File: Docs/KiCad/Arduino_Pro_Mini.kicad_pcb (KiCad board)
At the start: 2 copper layers, 47 x 95.2 mm, 19 parts, among them P1 Digital, P2 COM, P3 ADC, P4 Analog, P5 ADC, P6 COM, P7 CONN_01X04, P8 CONN_01X03, P9 CONN_01X04, SW1 SW_PUSH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

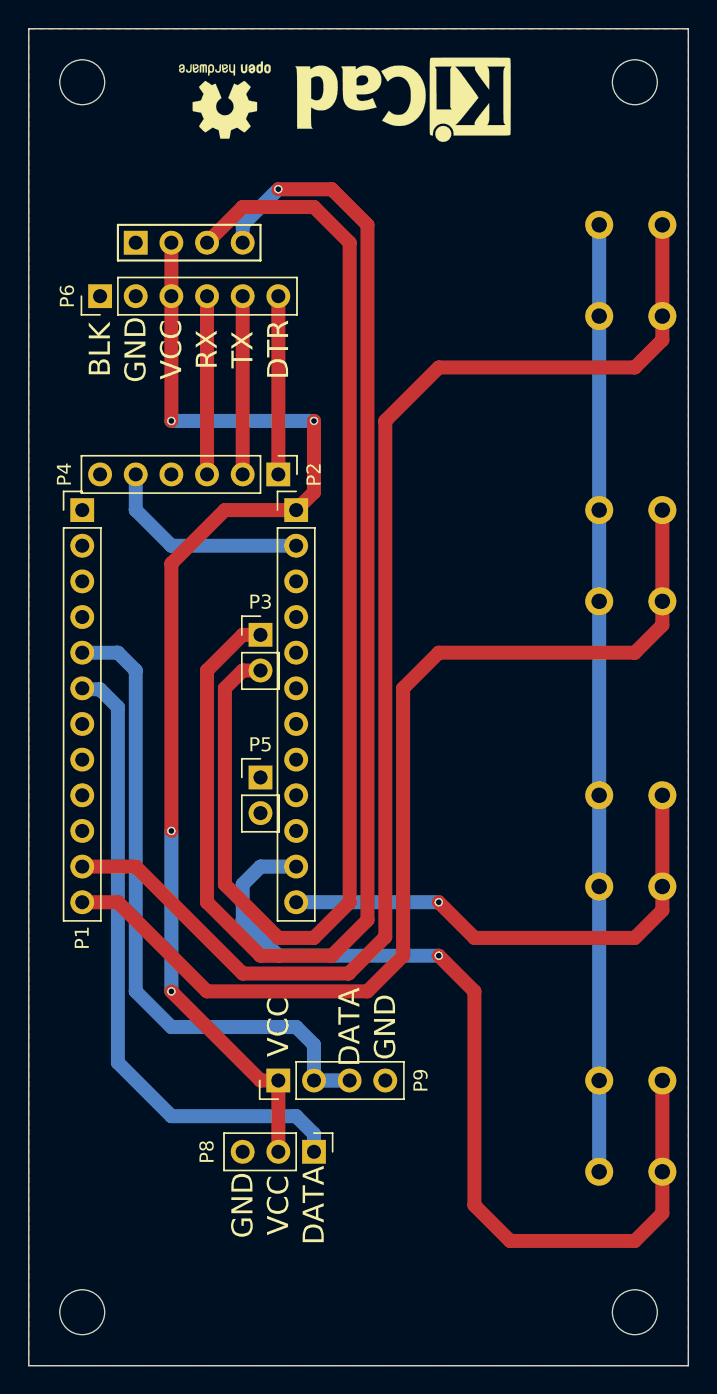
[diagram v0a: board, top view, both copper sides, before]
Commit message: Reducida tamaño PCB
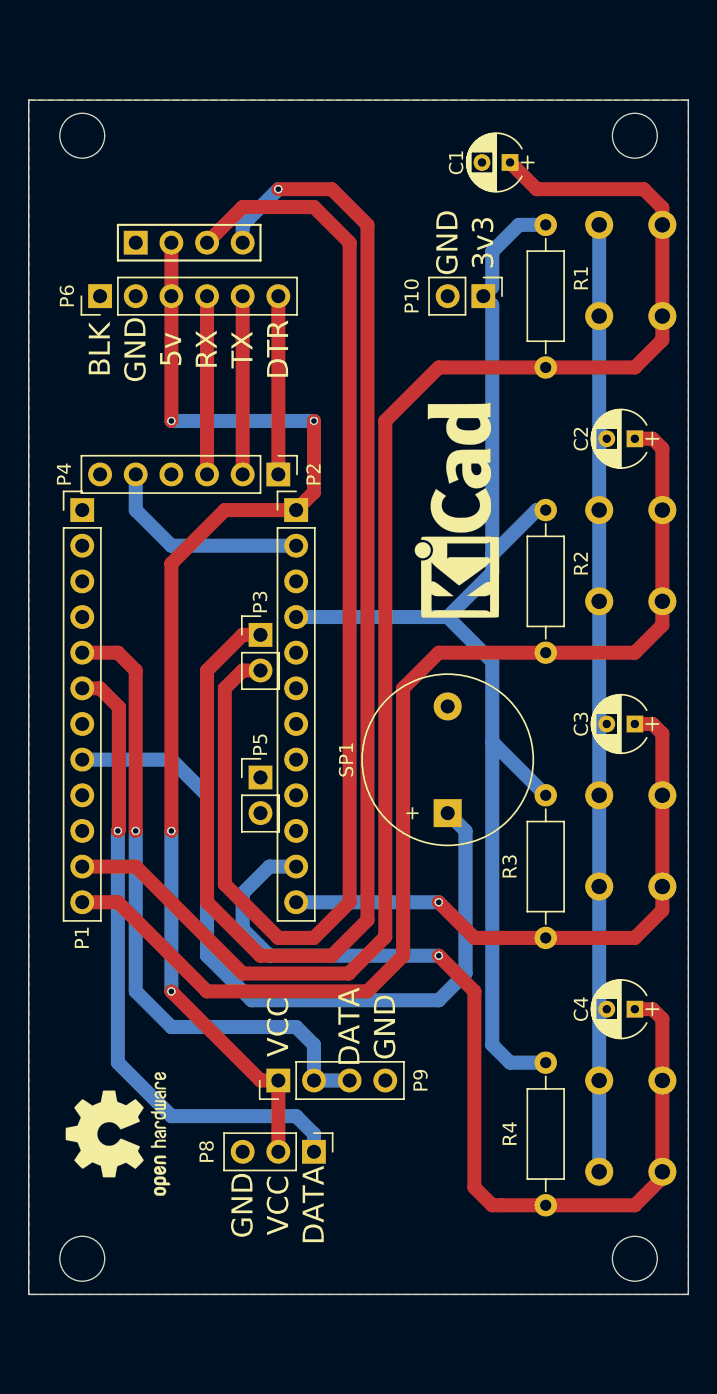
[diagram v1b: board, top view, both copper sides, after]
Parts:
- removed the REF*** at (148.6, 63.5)
- added C1: 1uF, Capacitors_ThroughHole:CP_Radial_D4.0mm_P2.00mm, F.Cu at (168.9, 67.9)
- added C2: 1uF, Capacitors_ThroughHole:CP_Radial_D4.0mm_P2.00mm, F.Cu at (177.8, 87.6)
- added C3: 1uF, Capacitors_ThroughHole:CP_Radial_D4.0mm_P2.00mm, F.Cu at (177.8, 108.0)
- added C4: 1uF, Capacitors_ThroughHole:CP_Radial_D4.0mm_P2.00mm, F.Cu at (177.8, 128.3)
- added P10: CONN_01X02, Pin_Headers:Pin_Header_Straight_1x02_Pitch2.54mm, F.Cu at (167.0, 77.5)
- added R1: 15k, Resistors_ThroughHole:R_Axial_DIN0207_L6.3mm_D2.5mm_P10.16mm_Horizontal, F.Cu at (171.4, 72.4)
- added R2: 15k, Resistors_ThroughHole:R_Axial_DIN0207_L6.3mm_D2.5mm_P10.16mm_Horizontal, F.Cu at (171.4, 92.7)
- added R3: 15k, Resistors_ThroughHole:R_Axial_DIN0207_L6.3mm_D2.5mm_P10.16mm_Horizontal, F.Cu at (171.4, 113.0)
- added R4: 15k, Resistors_ThroughHole:R_Axial_DIN0207_L6.3mm_D2.5mm_P10.16mm_Horizontal, F.Cu at (171.4, 132.1)
- added REF***: OSHW-Logo2_9.8x8mm_SilkScreen, Symbols:OSHW-Logo2_9.8x8mm_SilkScreen, F.Cu at (141.0, 137.2)
- added SP1: SPEAKER, Buzzers_Beepers:Buzzer_12x9.5RM7.6, F.Cu at (164.5, 114.3)
- moved REF*** 29.5 mm to (165.1, 92.7), turned to 90 degrees
- moved REF** 3.81 mm to (138.4, 66.0)
- moved REF** 3.81 mm to (177.8, 66.0)
- moved REF** 3.81 mm to (177.8, 146.1)
- moved REF** 3.81 mm to (138.4, 146.1)
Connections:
- net /10(**/SS) renamed /10
- net /11(**/MOSI) renamed /11
- net /3(**) renamed /3
- net /9(**) renamed /9
- P1 pad 8: Net-(P1-Pad8) -> /5
- P4 pad 4: Net-(P4-Pad4) -> /3.3v
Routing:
- net /3.3v: track 0.00 -> 89.9 mm
- net /5: track 0.00 -> 53.8 mm
- net /8: track 92.9 -> 106.3 mm
- net /9: track 74.1 -> 80.8 mm
- net /10: track 36.2 -> 42.8 mm, vias 3 -> 2
- net /11: track 65.5 -> 68.6 mm, vias 2 -> 1
- net /3: track 45.8 -> 46.0 mm, vias 1 -> 2
- net /2: vias 0 -> 1
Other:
- board size 47 x 95.2 mm -> 47 x 85.1 mm
- board text added: "3v3"
- board text added: "5v"
- board text added: "Developed by MickySimulation 2019"
- board text removed: "Developed by MickySimulation"
